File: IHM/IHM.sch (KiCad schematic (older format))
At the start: 2 parts

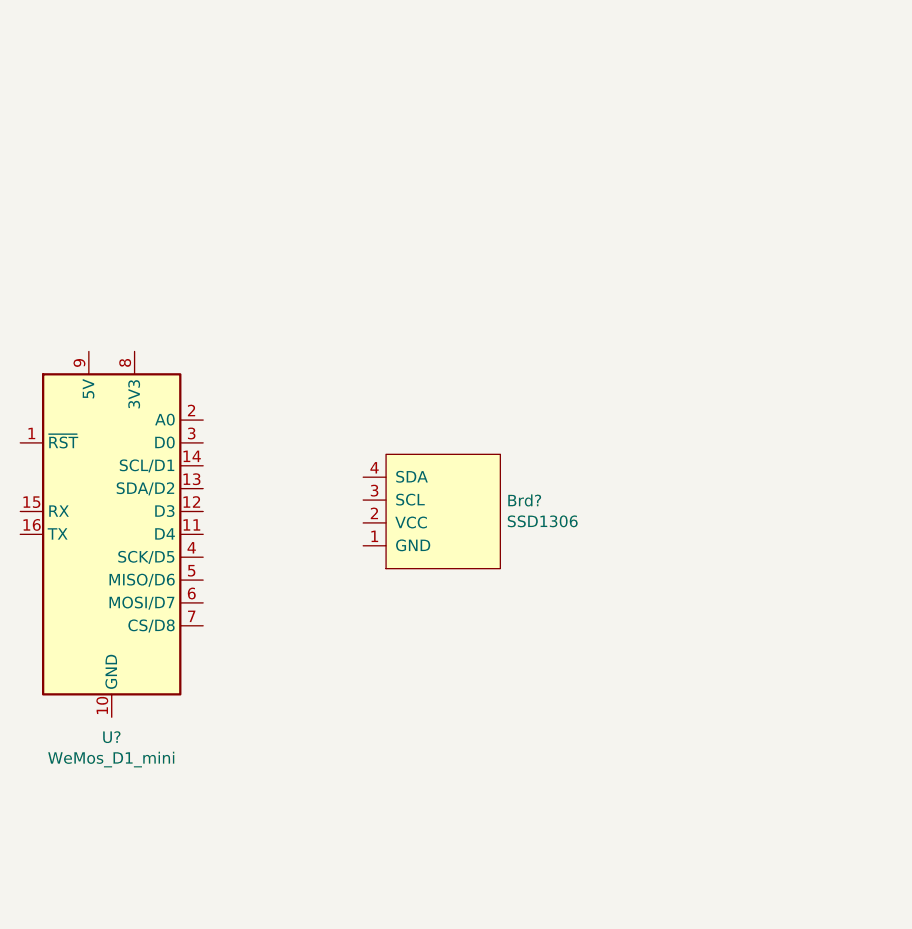
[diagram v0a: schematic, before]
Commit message: Schema + pcb de l'IHM
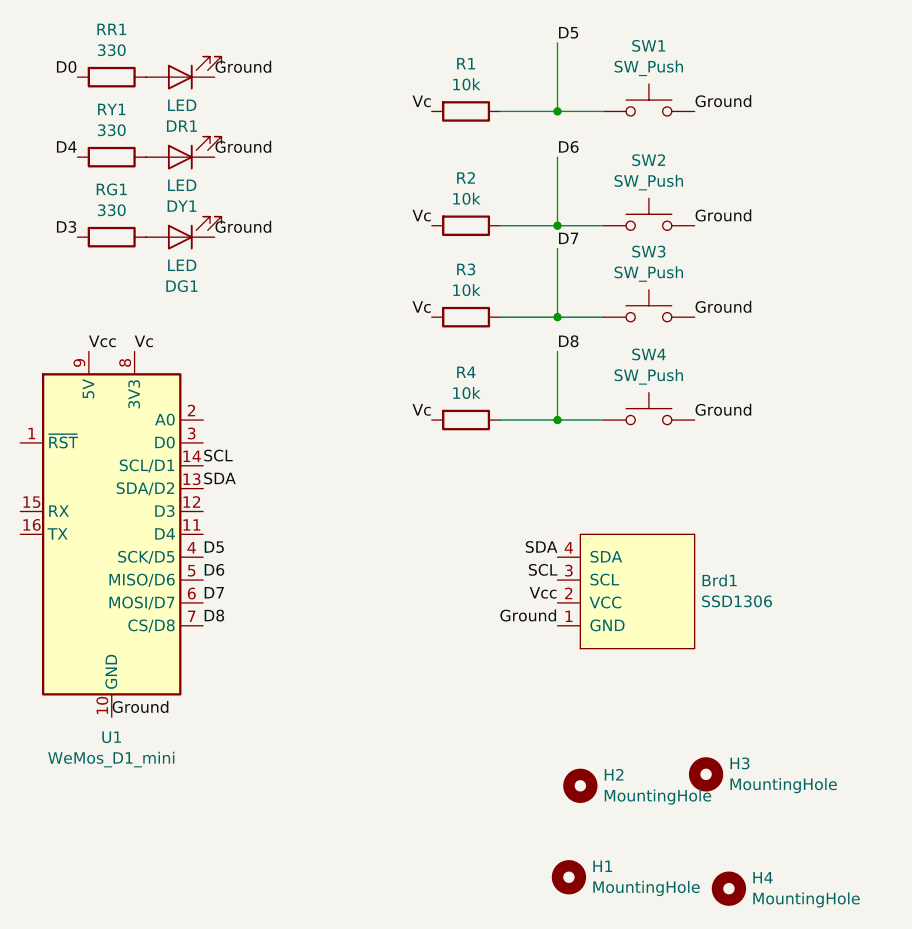
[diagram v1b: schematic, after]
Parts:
- added DG1, DR1, DY1: LED, LED_THT:LED_D3.0mm, symbol Device:LED
- added H1, H2, H3, H4: MountingHole, MountingHole:MountingHole_3.2mm_M3, symbol Mechanical:MountingHole
- added R1, R2, R3, R4: 10k, Resistor_SMD:R_0805_2012Metric, symbol Device:R
- added RG1, RR1, RY1: 330, Resistor_SMD:R_0805_2012Metric, symbol Device:R
- added SW1, SW2, SW3, SW4: SW_Push, Button_Switch_THT:SW_PUSH_6mm_H4.3mm, symbol Switch:SW_Push
- gave numbers to parts that had none: 2
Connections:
- net Ground: now reaches U1.10 (GND)
- net Ground: now also Brd1.1 (GND), DG1.1 (K), DR1.1 (K), DY1.1 (K), SW1.2, SW2.2, SW3.2, SW4.2
- net SDA: now reaches U1.13 (SDA/D2)
- net SDA: now also Brd1.4 (SDA)
- net SCL: now reaches U1.14 (SCL/D1)
- net SCL: now also Brd1.3 (SCL)
- net D5: now reaches U1.4 (SCK/D5)
- net D5: now also R1.1, SW1.1
- net D6: now reaches U1.5 (MISO/D6)
- net D6: now also R2.1, SW2.1
- net D7: now reaches U1.6 (MOSI/D7)
- net D7: now also R3.1, SW3.1
- net D8: now reaches U1.7 (CS/D8)
- net D8: now also R4.1, SW4.1
- net Vc: now reaches U1.8 (3V3)
- net Vc: now also R1.2, R2.2, R3.2, R4.2
- net Vcc: now reaches U1.9 (5V)
- net Vcc: now also Brd1.2 (VCC)
- new net: DR1.2 (A), RR1.1
- new net: DY1.2 (A), RY1.1
- new net: DG1.2 (A), RG1.1
- new net D0: RR1.2
- new net D3: RG1.2
- new net D4: RY1.2
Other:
- moved on the sheet: Brd1

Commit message: Replace power symbols
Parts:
- Brd1: symbol UTCoupe:SSD1306 -> IHM-rescue:SSD1306-UTCoupe
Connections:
- net labels added: +3V3, +5V, GND
- net labels removed: Vc, Vcc
- wire segments 12 -> 34
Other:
- moved on the sheet: DR1, DY1, H1, H2, H3, H4, R1, R2, R3, R4, RR1, RY1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

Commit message: Change push button logic
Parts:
- removed Brd1: SSD1306, UTCoupe:128x64OLED, symbol IHM-rescue:SSD1306-UTCoupe
- added Brd1: SSD1306, UTCoupe:128x64OLED, symbol UTCoupe:SSD1306
- R1, R2, R3, R4, RG1, RR1, RY1: footprint Resistor_SMD:R_0805_2012Metric -> Resistor_SMD:R_0603_1608Metric
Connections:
- wire segments 34 -> 10
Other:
- moved on the sheet: R1, SW1

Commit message: Change led resistor values
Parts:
- RG1, RR1, RY1: value 330 -> 3k3
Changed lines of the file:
@@
 P 5450 950
 F 0 "RR1" V 5243 950 50  0000 C CNN
-F 1 "330" V 5334 950 50  0000 C CNN
+F 1 "3k3" V 5334 950 50  0000 C CNN
 F 2 "Resistor_SMD:R_0603_1608Metric" V 5380 950 50  0001 C CNN
 F 3 "~" H 5450 950 50  0001 C CNN
@@
 P 5450 1400
 F 0 "RY1" V 5243 1400 50  0000 C CNN
-F 1 "330" V 5334 1400 50  0000 C CNN
+F 1 "3k3" V 5334 1400 50  0000 C CNN
 F 2 "Resistor_SMD:R_0603_1608Metric" V 5380 1400 50  0001 C CNN
 F 3 "~" H 5450 1400 50  0001 C CNN
@@
 P 5450 1850
 F 0 "RG1" V 5243 1850 50  0000 C CNN
-F 1 "330" V 5334 1850 50  0000 C CNN
+F 1 "3k3" V 5334 1850 50  0000 C CNN
 F 2 "Resistor_SMD:R_0603_1608Metric" V 5380 1850 50  0001 C CNN
 F 3 "~" H 5450 1850 50  0001 C CNN

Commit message: Add jack connector
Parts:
- added J?: JACK, symbol Connector_Generic:Conn_01x02
- added R?: 10k, Resistor_SMD:R_0603_1608Metric, symbol Device:R
- SW1: value SW_Push -> BTN_R1
- SW2: value SW_Push -> BTN_L1
- SW3: value SW_Push -> BTN_L2
- SW4: value SW_Push -> BTN_R2
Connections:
- net +3V3: now also R?.2
- net D0: now also R4.1, SW4.1; no longer RR1.2
- net D3: now also RR1.2; no longer RG1.2
- net D4: now also U1.11 (D4), J?.1 (Pin_1), R?.1
- net D8: now also RG1.2; no longer R4.1, SW4.1
- net GND: now also J?.2 (Pin_2)
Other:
- moved on the sheet: Brd1

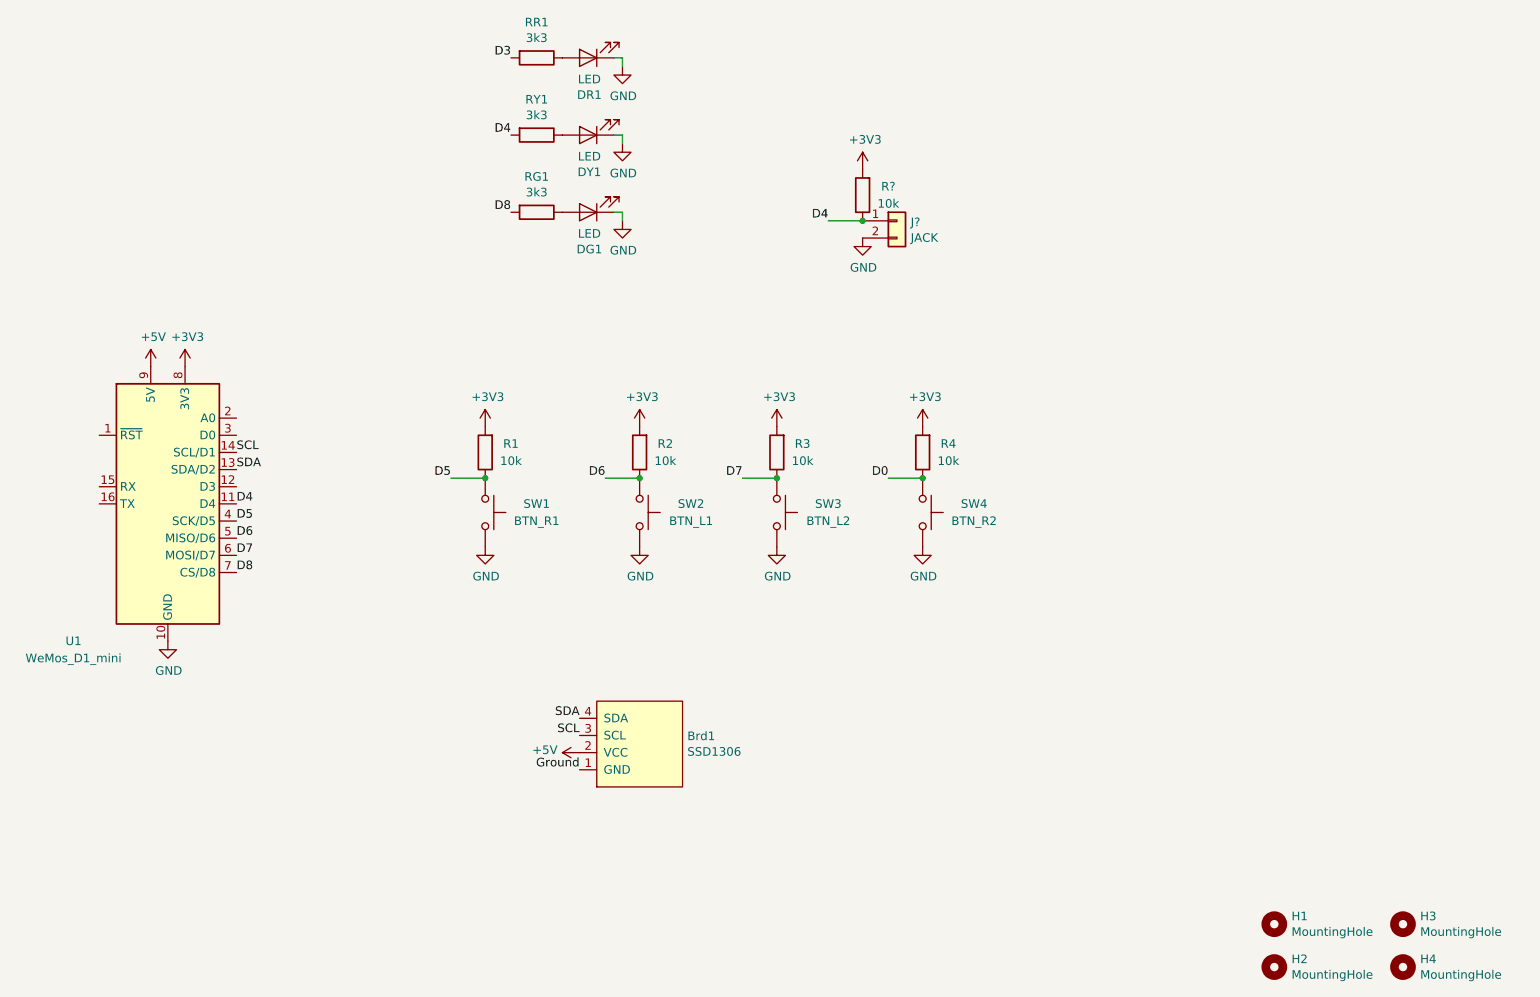
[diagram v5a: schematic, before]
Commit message: Add I2C pull ups and capacitor on switches
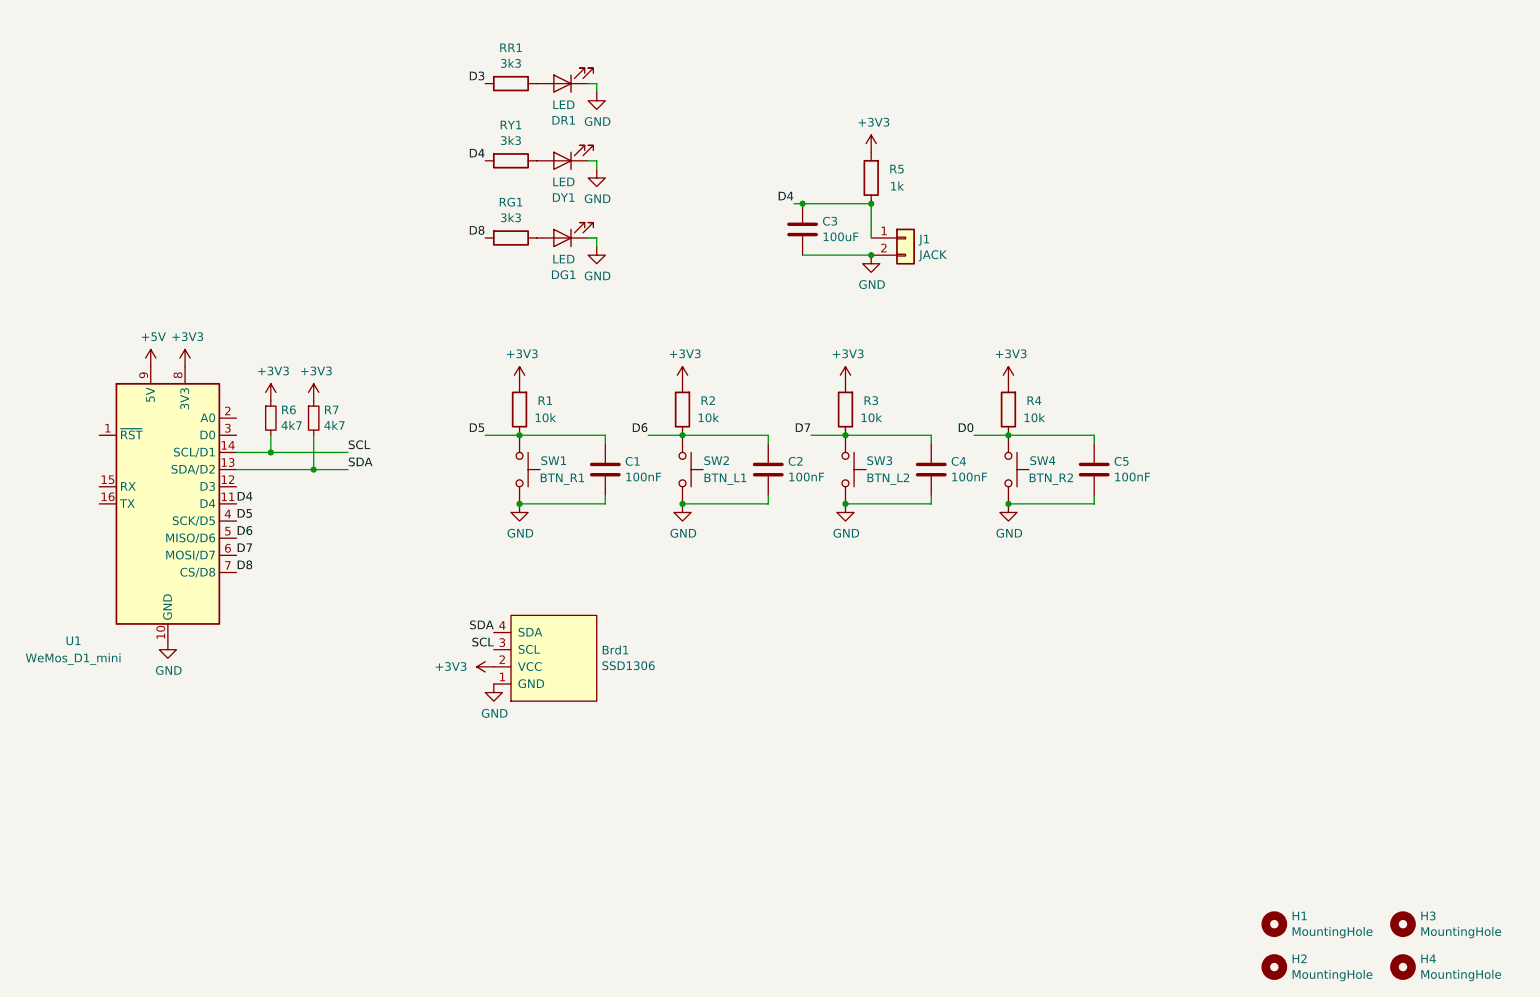
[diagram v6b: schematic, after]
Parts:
- added C1, C2, C4, C5: 100nF, Capacitor_SMD:C_0603_1608Metric, symbol Device:C
- added C3: 100uF, Capacitor_SMD:C_0603_1608Metric, symbol Device:C
- added R6, R7: 4k7, Resistor_SMD:R_0603_1608Metric, symbol Device:R_Small
- J1: renamed from J?; footprint (none) -> Connector_Phoenix_MC:PhoenixContact_MC_1,5_2-G-3.5_1x02_P3.50mm_Horizontal
- R5: renamed from R?; value 10k -> 1k
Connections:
- net Ground is gone; now on net GND: Brd1.1 (GND)
- net +3V3: now also Brd1.2 (VCC), R6.1, R7.1
- net +5V: no longer Brd1.2 (VCC)
- net D0: now also C5.1
- net D4: now also C3.1
- net D5: now also C1.1
- net D6: now also C2.1
- net D7: now also C4.1
- net GND: now also C1.2, C2.2, C3.2, C4.2, C5.2
- net SCL: now also R6.2
- net SDA: now also R7.2
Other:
- moved on the sheet: Brd1, DG1, DR1, DY1, J1, R1, R2, R3, R4, R5, RG1, RR1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

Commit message: Change led res val
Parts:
- removed DY1: LED, LED_THT:LED_D3.0mm, symbol Device:LED
- removed RY1: 3k3, Resistor_SMD:R_0603_1608Metric, symbol Device:R
- C3: value 100uF -> 100nF
- R5: value 1k -> 10k
- RG1, RR1: value 3k3 -> 1k5
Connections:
- net D0: now also U1.3 (D0)
- net D3: now also U1.12 (D3)
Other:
- moved on the sheet: DG1, RG1
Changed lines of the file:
@@
 P 5300 1100
 F 0 "RR1" V 5093 1100 50  0000 C CNN
-F 1 "3k3" V 5184 1100 50  0000 C CNN
+F 1 "1k5" V 5184 1100 50  0000 C CNN
 F 2 "Resistor_SMD:R_0603_1608Metric" V 5230 1100 50  0001 C CNN
 F 3 "~" H 5300 1100 50  0001 C CNN
@@
 	0    1    1    0
 $EndComp
-$Comp
-L Device:R RY1
-U 1 1 60A23B0E
-P 5300 1550
-F 0 "RY1" V 5093 1550 50  0000 C CNN
-F 1 "3k3" V 5184 1550 50  0000 C CNN
-F 2 "Resistor_SMD:R_0603_1608Metric" V 5230 1550 50  0001 C CNN
-F 3 "~" H 5300 1550 50  0001 C CNN
-	1    5300 1550
-	0    1    1    0
-$EndComp
-Text Label 5150 1550 2    50   ~ 0
-D4
 $Comp
 L Mechanical:MountingHole H3
@@
 L power:GND #PWR0104
 U 1 1 60B3BA0E
-P 5800 2050
-F 0 "#PWR0104" H 5800 1800 50  0001 C CNN
-F 1 "GND" H 5805 1877 50  0000 C CNN
-F 2 "" H 5800 2050 50  0001 C CNN
-F 3 "" H 5800 2050 50  0001 C CNN
-	1    5800 2050
+P 5800 1650
+F 0 "#PWR0104" H 5800 1400 50  0001 C CNN
+F 1 "GND" H 5805 1477 50  0000 C CNN
+F 2 "" H 5800 1650 50  0001 C CNN
+F 3 "" H 5800 1650 50  0001 C CNN
+	1    5800 1650
 	1    0    0    -1
 $EndComp
@@
 L Device:R RG1
 U 1 1 60A2494E
-P 5300 2000
-F 0 "RG1" V 5093 2000 50  0000 C CNN
-F 1 "3k3" V 5184 2000 50  0000 C CNN
-F 2 "Resistor_SMD:R_0603_1608Metric" V 5230 2000 50  0001 C CNN
-F 3 "~" H 5300 2000 50  0001 C CNN
-	1    5300 2000
+P 5300 1600
+F 0 "RG1" V 5093 1600 50  0000 C CNN
+F 1 "1k5" V 5184 1600 50  0000 C CNN
+F 2 "Resistor_SMD:R_0603_1608Metric" V 5230 1600 50  0001 C CNN
+F 3 "~" H 5300 1600 50  0001 C CNN
+	1    5300 1600
 	0    1    1    0
 $EndComp
 Wire Wire Line
-	5750 2000 5800 2000
-Wire Wire Line
-	5800 2000 5800 2050
-$Comp
-L power:GND #PWR0105
-U 1 1 60B492D7
-P 5800 1600
-F 0 "#PWR0105" H 5800 1350 50  0001 C CNN
-F 1 "GND" H 5805 1427 50  0000 C CNN
-F 2 "" H 5800 1600 50  0001 C CNN
-F 3 "" H 5800 1600 50  0001 C CNN
-	1    5800 1600
-	1    0    0    -1
-$EndComp
-Wire Wire Line
-	5750 1550 5800 1550
-Wire Wire Line
-	5800 1550 5800 1600
+	5750 1600 5800 1600
+Wire Wire Line
+	5800 1600 5800 1650
 $Comp
 L power:GND #PWR0106
@@
 	7050 3150 7250 3150
 Connection ~ 7250 3150
-Text Label 5150 2000 2    50   ~ 0
+Text Label 5150 1600 2    50   ~ 0
 D8
 $Comp
@@
 P 7400 1650
 F 0 "R5" H 7250 1600 50  0000 C CNN
-F 1 "1k" H 7250 1700 50  0000 C CNN
+F 1 "10k" H 7250 1700 50  0000 C CNN
 F 2 "Resistor_SMD:R_0603_1608Metric" V 7330 1650 50  0001 C CNN
 F 3 "~" H 7400 1650 50  0001 C CNN
@@
 L Device:LED DG1
 U 1 1 60A24948
-P 5600 2000
-F 0 "DG1" H 5593 2216 50  0000 C CNN
-F 1 "LED" H 5593 2125 50  0000 C CNN
-F 2 "LED_THT:LED_D3.0mm" H 5600 2000 50  0001 C CNN
-F 3 "~" H 5600 2000 50  0001 C CNN
-	1    5600 2000
-	-1   0    0    1
-$EndComp
-$Comp
-L Device:LED DY1
-U 1 1 60A23B08
-P 5600 1550
-F 0 "DY1" H 5593 1766 50  0000 C CNN
-F 1 "LED" H 5593 1675 50  0000 C CNN
-F 2 "LED_THT:LED_D3.0mm" H 5600 1550 50  0001 C CNN
-F 3 "~" H 5600 1550 50  0001 C CNN
-	1    5600 1550
+P 5600 1600
+F 0 "DG1" H 5593 1816 50  0000 C CNN
+F 1 "LED" H 5593 1725 50  0000 C CNN
+F 2 "LED_THT:LED_D3.0mm" H 5600 1600 50  0001 C CNN
+F 3 "~" H 5600 1600 50  0001 C CNN
+	1    5600 1600
 	-1   0    0    1
 $EndComp
@@
 P 7000 1950
 F 0 "C3" H 7115 1996 50  0000 L CNN
-F 1 "100uF" H 7115 1905 50  0000 L CNN
+F 1 "100nF" H 7115 1905 50  0000 L CNN
 F 2 "Capacitor_SMD:C_0603_1608Metric" H 7038 1800 50  0001 C CNN
 F 3 "~" H 7000 1950 50  0001 C CNN
@@
 Text Label 8000 3150 2    50   ~ 0
 D0
+Text Label 3700 3150 0    50   ~ 0
+D0
+Text Label 3700 3450 0    50   ~ 0
+D3
 $EndSCHEMATC

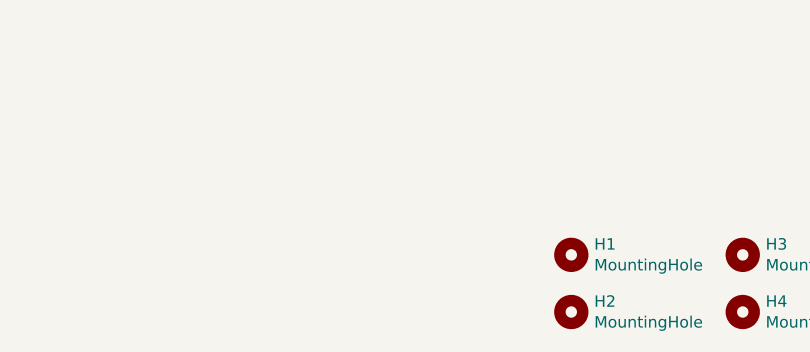
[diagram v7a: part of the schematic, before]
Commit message: Add mounting holes
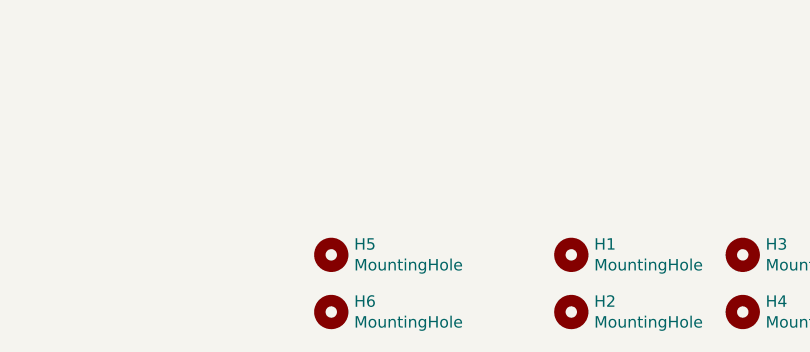
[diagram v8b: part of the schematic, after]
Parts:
- added H5, H6: MountingHole, MountingHole:MountingHole_2.2mm_M2, symbol Mechanical:MountingHole
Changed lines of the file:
@@
 Text Label 3700 3450 0    50   ~ 0
 D3
+$Comp
+L Mechanical:MountingHole H5
+U 1 1 60CCDBFA
+P 8700 6000
+F 0 "H5" H 8800 6046 50  0000 L CNN
+F 1 "MountingHole" H 8800 5955 50  0000 L CNN
+F 2 "MountingHole:MountingHole_2.2mm_M2" H 8700 6000 50  0001 C CNN
+F 3 "~" H 8700 6000 50  0001 C CNN
+	1    8700 6000
+	1    0    0    -1
+$EndComp
+$Comp
+L Mechanical:MountingHole H6
+U 1 1 60CCDC00
+P 8700 6250
+F 0 "H6" H 8800 6296 50  0000 L CNN
+F 1 "MountingHole" H 8800 6205 50  0000 L CNN
+F 2 "MountingHole:MountingHole_2.2mm_M2" H 8700 6250 50  0001 C CNN
+F 3 "~" H 8700 6250 50  0001 C CNN
+	1    8700 6250
+	1    0    0    -1
+$EndComp
 $EndSCHEMATC
